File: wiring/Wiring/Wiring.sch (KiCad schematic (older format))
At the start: 9 parts, among them U1 MAIN, U2 E, U3 F, U4 G

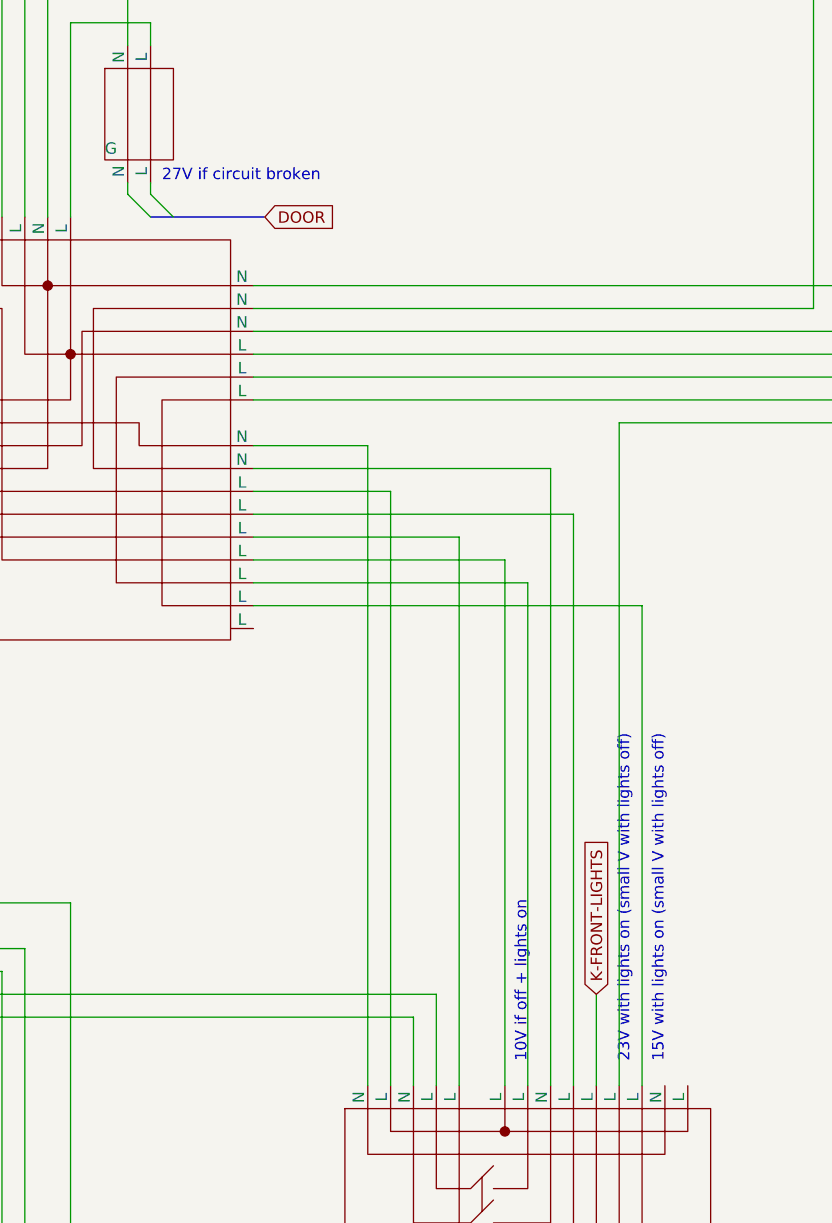
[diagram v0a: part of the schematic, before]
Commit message: Remove remarks about phantom voltage
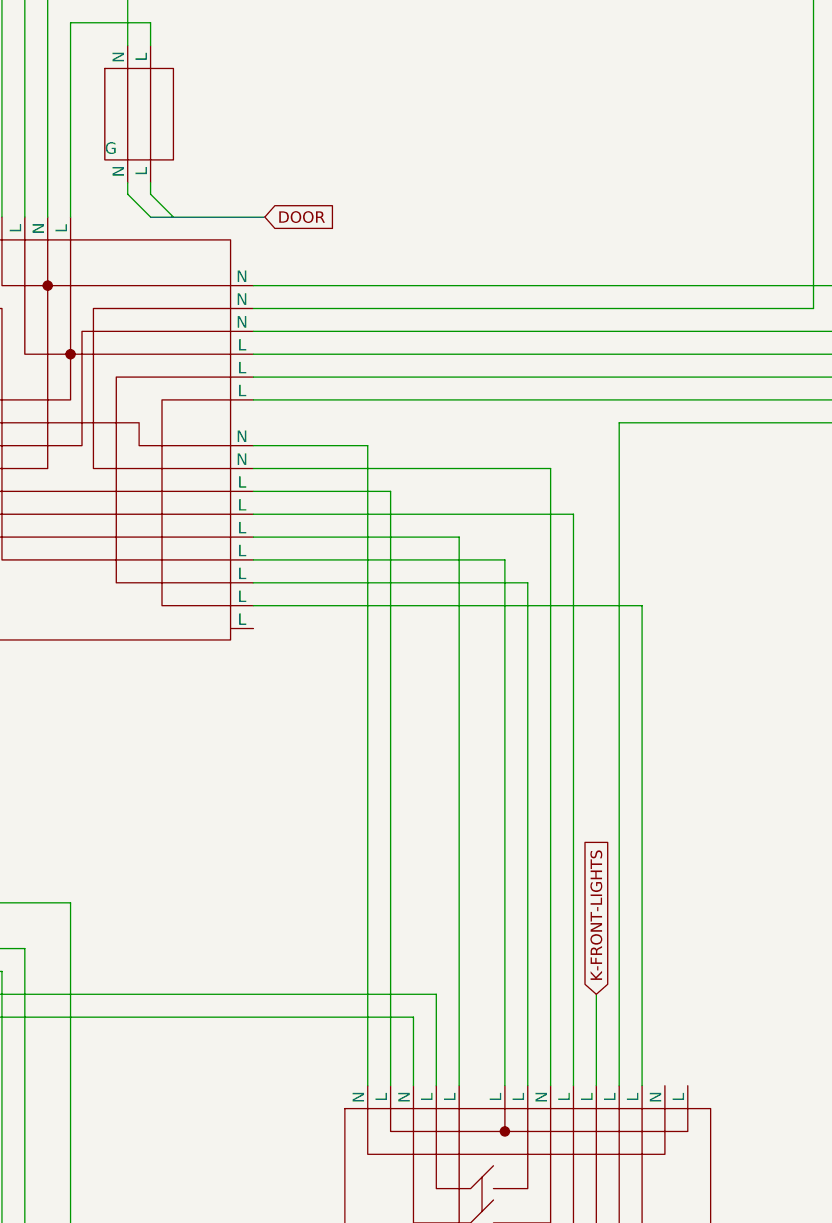
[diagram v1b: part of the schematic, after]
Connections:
- net at U3.9 (N): now also U2.17 (N)
- net at U3.~ (L): now also U2.24 (L)
- net at U2.24 (L): no longer U3.~ (L)
- net at U1.~ (N): now also U?.16 (N)
- net at U?.16 (N): no longer U1.~ (N)
- net at U?.~ (N): now also U?.12 (L)
- new net: U2.14 (L), U?.12 (L)
- new net: U?.10 (N), U?.8 (N) (x2)
- new net: U?.12 (L), U?.9 (L) (x2)
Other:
- note removed: "10V if off + lights on"
- note removed: "15V with lights on (small V with lights off)"
- note removed: "23V with lights on (small V with lights off)"
- note removed: "27V if circuit broken"
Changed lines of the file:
@@
 Text GLabel 13000 8000 1    50   Input ~ 0
 K-FRONT-LIGHTS
-Text Notes 12700 8300 1    50   ~ 0
-10V if off + lights on
-Text Notes 13150 8300 1    50   ~ 0
-23V with lights on (small V with lights off)
 Wire Wire Line
 	10300 8100 12200 8100
@@
 Wire Wire Line
 	12400 6000 12400 8400
-Text Notes 11100 4450 0    50   ~ 0
-27V if circuit broken
 Wire Notes Line
 	15600 6750 16100 6750
@@
 	-1   0    0    1
 $EndComp
-Text Notes 13300 8300 1    50   ~ 0
-15V with lights on (small V with lights off)
 Wire Wire Line
 	14450 5400 14450 2150

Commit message: Connect L, U, V
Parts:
- added U?: L, symbol Wiring:L
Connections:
- net at U3.9 (N): now also U?.12 (N)
- net at U3.~ (L): now also U?.10 (N)
- net at U2.24 (L): no longer U3.~ (L)
- net at U1.~ (N): now also U?.16 (N)
- net at U?.16 (N): no longer U1.~ (N)
- net at U?.~ (N): now also U?.12 (L)
- new net: U2.24 (L), U3.~ (L)
- new net: U2.14 (L), U?.12 (L)
- new net: U?.10 (N), U?.8 (N) (x2)
- new net: U?.12 (L), U?.9 (L) (x2)
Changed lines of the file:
@@
 Wire Wire Line
 	14550 2950 15800 2950
+$Comp
+L Wiring:L U?
+U 1 1 5EE0BFE0
+P 15250 6250
+F 0 "U?" H 15100 6400 50  0001 C CNN
+F 1 "L" H 15250 6523 50  0000 C CNN
+F 2 "" H 14550 6100 50  0001 C CNN
+F 3 "" H 14550 6100 50  0001 C CNN
+	1    15250 6250
+	1    0    0    -1
+$EndComp
+Wire Wire Line
+	13400 8400 13400 6300
+Wire Wire Line
+	13400 6300 14950 6300
+Wire Wire Line
+	13300 6200 14950 6200
+Wire Wire Line
+	13300 6200 13300 8400
+Wire Wire Line
+	15550 6200 15650 6200
+Wire Wire Line
+	15550 6300 15750 6300
+Wire Wire Line
+	15750 6300 15750 6200
+Entry Wire Line
+	15650 6200 15750 6100
+Entry Wire Line
+	15750 6200 15850 6100
 Wire Bus Line
 	10850 1850 11400 1850
@@
 Wire Bus Line
 	11050 4600 11550 4600
+Wire Bus Line
+	15750 6100 15950 6100
+Text GLabel 15950 6100 2    50   Input ~ 0
+LASER-LAB
 $EndSCHEMATC

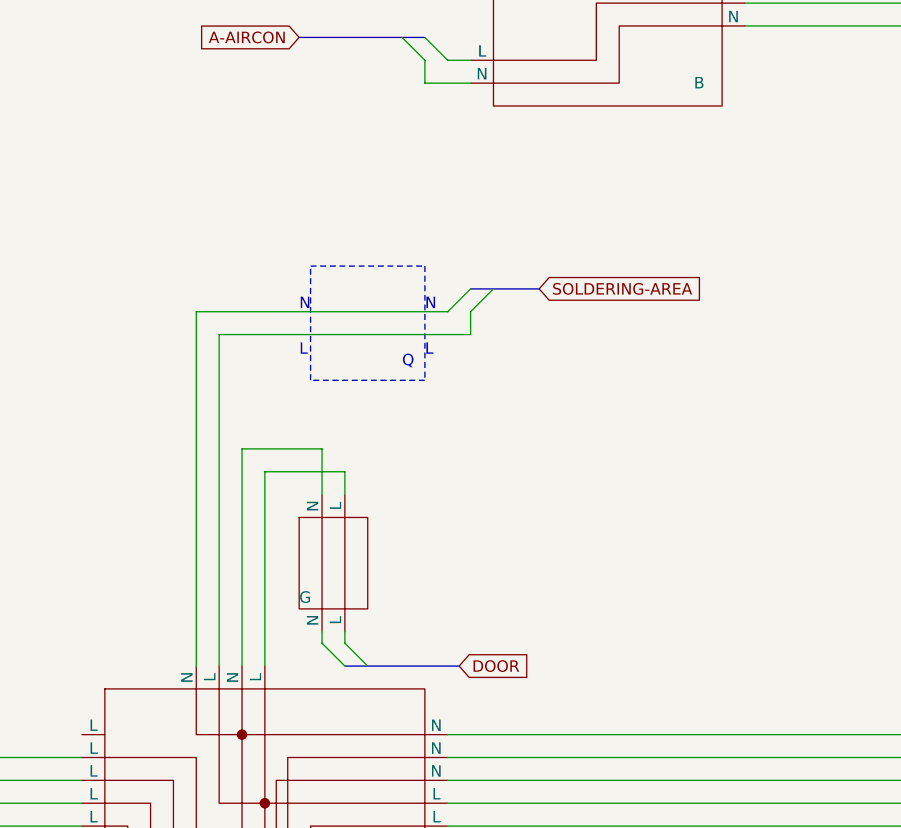
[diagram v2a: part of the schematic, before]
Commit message: Add symbol for Q
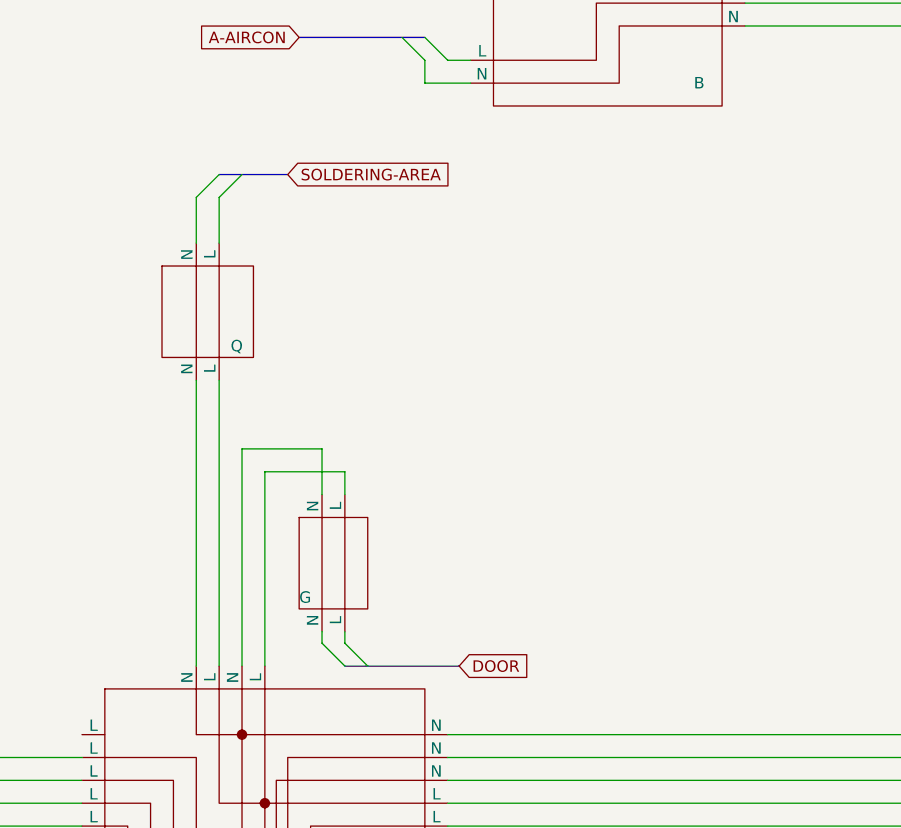
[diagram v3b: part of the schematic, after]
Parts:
- added U?: Q, symbol Wiring:Q
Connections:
- net at U3.~ (L): now also U?.10 (N); no longer U2.24 (L)
- net at U?.10 (N): no longer U3.~ (L)
- net at U2.~ (N): now also U?.12 (N)
- net at U1.~ (N): now also U?.16 (N)
- net at U?.16 (N): no longer U1.~ (N)
- net at U?.~ (N): now also U?.12 (L)
- new net: U2.24 (L), U3.~ (L)
- new net: U2.14 (L), U?.12 (L)
- new net: U2.~ (N), U?.10 (N)
- new net: U?.10 (N), U?.8 (N) (x2)
- new net: U?.12 (L), U?.9 (L) (x2)
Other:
- note removed: "Q"
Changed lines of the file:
@@
 Wire Wire Line
 	10700 7600 10700 11450
-Wire Notes Line
-	10900 2850 11400 2850
-Wire Notes Line
-	11400 2850 11400 3350
-Wire Notes Line
-	11400 3350 10900 3350
-Wire Notes Line
-	10900 3350 10900 2850
-Wire Wire Line
-	10500 4600 10500 3150
-Wire Wire Line
-	10400 4600 10400 3050
-Wire Wire Line
-	10400 3050 11500 3050
-Wire Wire Line
-	11600 3150 11600 3050
-Wire Wire Line
-	10500 3150 11600 3150
-Entry Wire Line
-	11500 3050 11600 2950
-Entry Wire Line
-	11600 3050 11700 2950
-Text GLabel 11900 2950 2    50   Input ~ 0
+Wire Wire Line
+	10500 4600 10500 3350
+Wire Wire Line
+	10400 4600 10400 3350
+Entry Wire Line
+	10400 2550 10500 2450
+Entry Wire Line
+	10500 2550 10600 2450
+Text GLabel 10800 2450 2    50   Input ~ 0
 SOLDERING-AREA
-Text Notes 11300 3300 0    50   ~ 0
-Q
-Text Notes 11400 3250 0    50   ~ 0
-L
-Text Notes 11400 3050 0    50   ~ 0
-N
-Text Notes 10850 3050 0    50   ~ 0
-N
-Text Notes 10850 3250 0    50   ~ 0
-L
 Wire Wire Line
 	11500 6100 12600 6100
@@
 Entry Wire Line
 	15750 6200 15850 6100
-Wire Bus Line
-	10850 1850 11400 1850
-Wire Bus Line
-	11600 2950 11900 2950
-Wire Bus Line
-	18000 7250 18350 7250
-Wire Bus Line
-	18000 6750 18350 6750
-Wire Bus Line
-	11900 700  12200 700
-Wire Bus Line
-	11050 4600 11550 4600
-Wire Bus Line
-	15750 6100 15950 6100
 Text GLabel 15950 6100 2    50   Input ~ 0
 LASER-LAB
+$Comp
+L Wiring:Q U?
+U 1 1 5EE2C972
+P 10450 3050
+F 0 "U?" H 10300 3200 50  0001 C CNN
+F 1 "Q" H 10550 2900 50  0000 L CNN
+F 2 "" H 9750 2900 50  0001 C CNN
+F 3 "" H 9750 2900 50  0001 C CNN
+	1    10450 3050
+	1    0    0    -1
+$EndComp
+Wire Wire Line
+	10500 2750 10500 2550
+Wire Wire Line
+	10400 2550 10400 2750
+Wire Bus Line
+	10850 1850 11400 1850
+Wire Bus Line
+	10500 2450 10800 2450
+Wire Bus Line
+	18000 7250 18350 7250
+Wire Bus Line
+	18000 6750 18350 6750
+Wire Bus Line
+	11900 700  12200 700
+Wire Bus Line
+	11050 4600 11550 4600
+Wire Bus Line
+	15750 6100 15950 6100
 $EndSCHEMATC

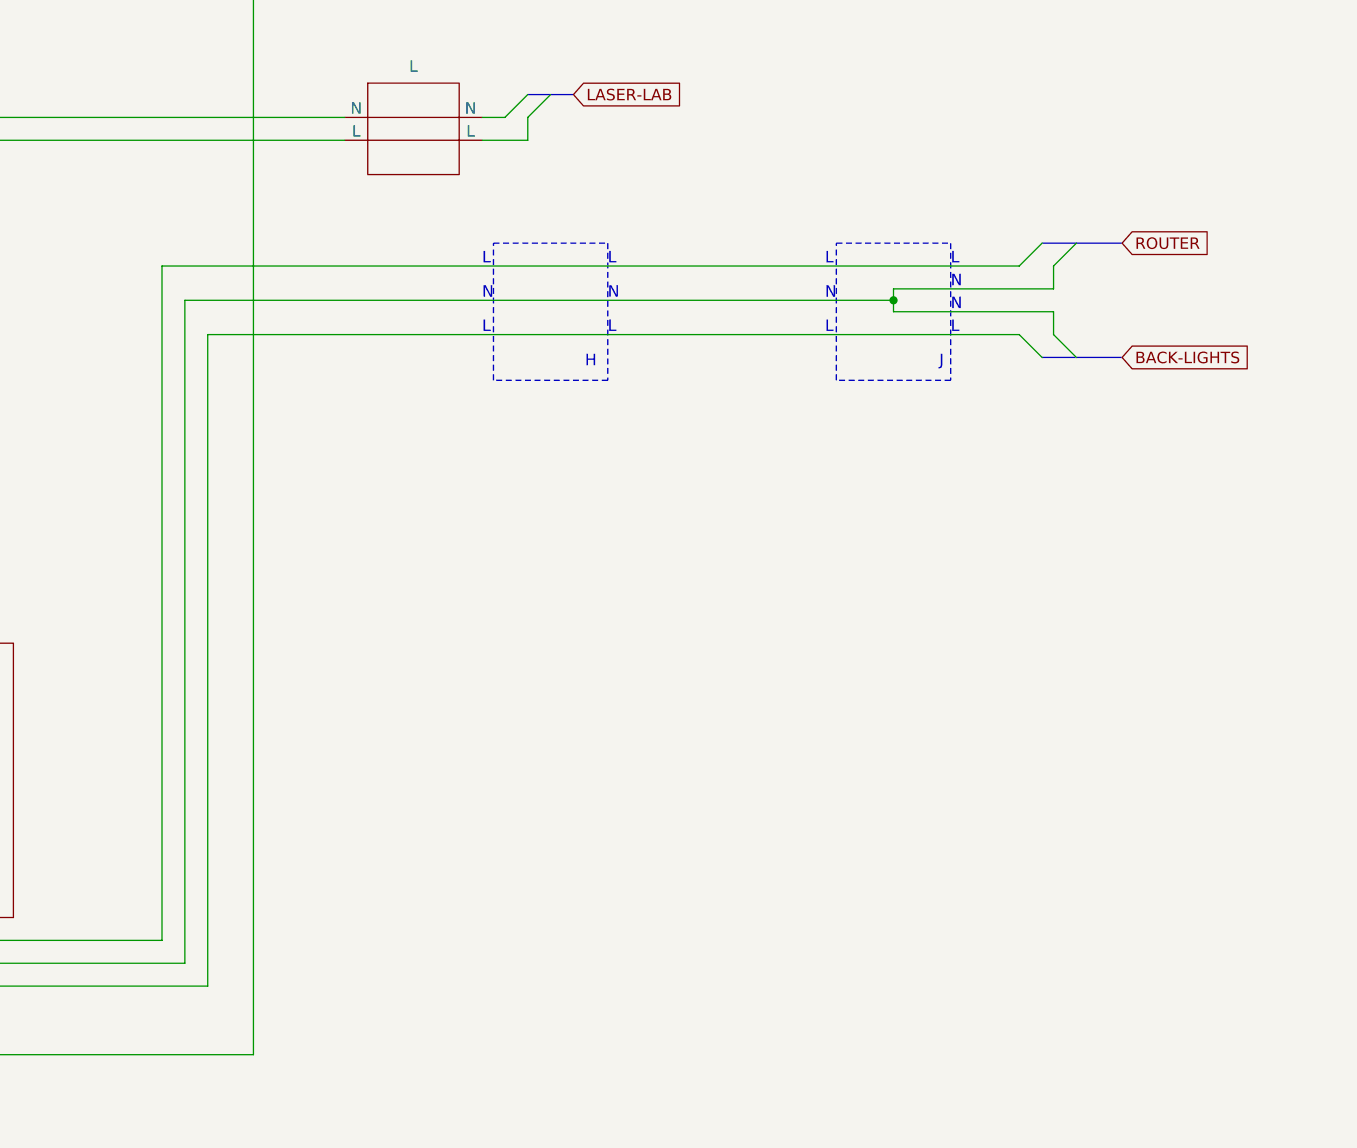
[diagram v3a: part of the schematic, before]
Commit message: Add symbol for J
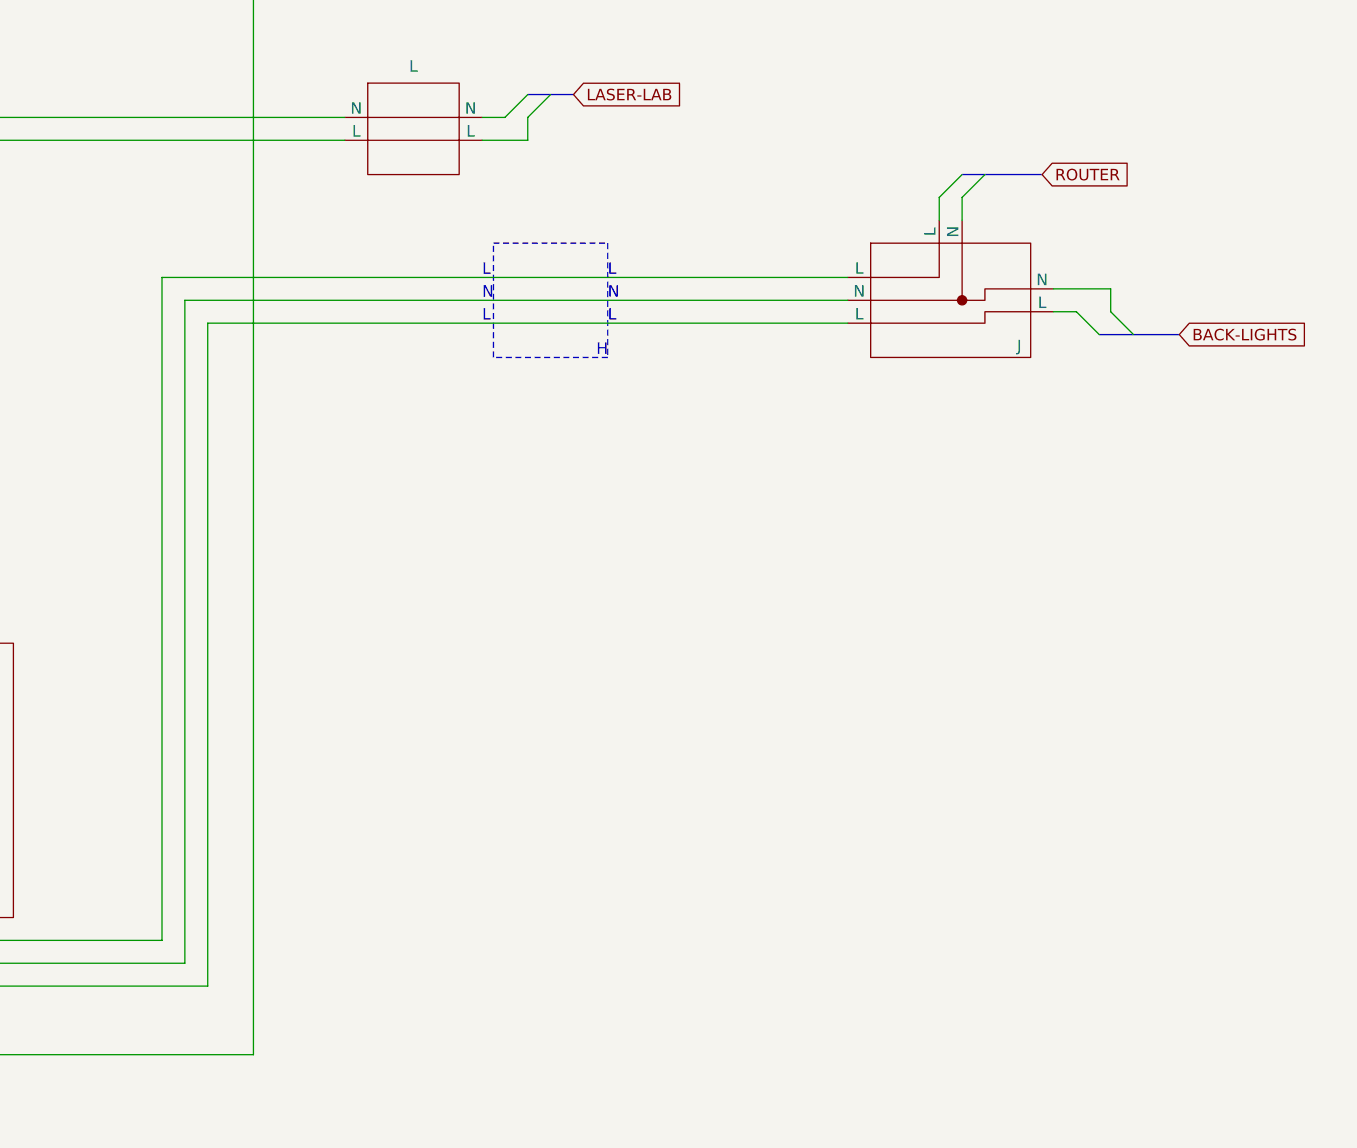
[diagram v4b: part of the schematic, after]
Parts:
- added U?: J, symbol Wiring:J
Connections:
- net at U3.~ (L): now also U?.10 (N); no longer U2.24 (L)
- net at U?.10 (N): no longer U3.~ (L)
- net at U2.6 (L): now also U?.10 (N)
- net at U2.8 (L): now also U?.10 (N)
- net at U2.~ (N): now also U?.12 (N); no longer U?.10 (N)
- net at U?.12 (N): no longer U2.~ (N)
- net at U1.~ (N): now also U?.16 (N)
- net at U?.16 (N): no longer U1.~ (N)
- net at U?.~ (N): now also U?.12 (L)
- new net: U2.24 (L), U3.~ (L)
- new net: U2.14 (L), U?.12 (L)
- new net: U2.~ (N), U?.10 (N)
- new net: U1.~ (N), U?.12 (N)
- new net: U?.10 (N), U?.8 (N) (x2)
- new net: U?.12 (L), U?.9 (L) (x2)
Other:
- note removed: "J"
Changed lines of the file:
@@
 	15600 6750 16100 6750
 Wire Notes Line
-	16100 6750 16100 7350
-Wire Notes Line
-	15600 7350 15600 6750
-Text Notes 16000 7300 0    50   ~ 0
-H
-Wire Notes Line
-	17100 6750 17600 6750
-Wire Notes Line
-	17600 6750 17600 7350
-Wire Notes Line
-	17600 7350 17100 7350
-Wire Notes Line
-	17100 7350 17100 6750
-Text Notes 17550 7300 0    50   ~ 0
-J
-Text GLabel 18350 6750 2    50   Input ~ 0
+	16100 6750 16100 7250
+Wire Notes Line
+	15600 7250 15600 6750
+Text GLabel 18000 6450 2    50   Input ~ 0
 ROUTER
 Entry Wire Line
-	17900 6850 18000 6750
-Entry Wire Line
-	18150 6750 18050 6850
-Wire Wire Line
-	18050 6950 18050 6850
+	17550 6550 17650 6450
+Entry Wire Line
+	17750 6450 17650 6550
 Wire Notes Line
 	11250 9750 11750 9750
@@
 Wire Wire Line
 	12900 5900 12900 8400
-Wire Notes Line
-	16100 7350 15600 7350
-Wire Wire Line
-	17350 6950 18050 6950
-Wire Wire Line
-	17350 7000 17350 6950
-Wire Wire Line
-	17350 7000 17350 7050
-Wire Wire Line
-	17350 7050 18050 7050
-Connection ~ 17350 7000
-Text Notes 17600 6850 0    50   ~ 0
+Text Notes 16100 6900 0    50   ~ 0
 L
-Text Notes 17600 6950 0    50   ~ 0
-N
-Text Notes 17600 7050 0    50   ~ 0
-N
-Text Notes 17600 7150 0    50   ~ 0
-L
-Text Notes 17050 6850 0    50   ~ 0
-L
-Text Notes 17050 7000 0    50   ~ 0
-N
-Text Notes 17050 7150 0    50   ~ 0
-L
-Text Notes 16100 6850 0    50   ~ 0
-L
-Text Notes 16100 7150 0    50   ~ 0
+Text Notes 16100 7100 0    50   ~ 0
 L
 Text Notes 16100 7000 0    50   ~ 0
@@
 Text Notes 15550 7000 0    50   ~ 0
 N
-Text Notes 15550 6850 0    50   ~ 0
+Text Notes 15550 6900 0    50   ~ 0
 L
-Text Notes 15550 7150 0    50   ~ 0
+Text Notes 15550 7100 0    50   ~ 0
 L
-Text GLabel 18350 7250 2    50   Input ~ 0
+Text GLabel 18600 7150 2    50   Input ~ 0
 BACK-LIGHTS
 Entry Wire Line
-	17900 7150 18000 7250
-Entry Wire Line
-	18050 7150 18150 7250
-Wire Wire Line
-	18050 7050 18050 7150
+	18150 7050 18250 7150
+Entry Wire Line
+	18300 7050 18400 7150
 Wire Wire Line
 	12300 8400 12300 8000
@@
 Wire Wire Line
 	10600 9900 14250 9900
-Wire Wire Line
-	14350 7150 14350 10000
-Wire Wire Line
-	14150 6850 14150 9800
 Wire Wire Line
 	9900 5200 9000 5200
@@
 	10800 10300 10800 11450
 Wire Wire Line
-	14150 6850 17900 6850
-Wire Wire Line
-	14250 7000 17350 7000
-Wire Wire Line
-	14350 7150 17900 7150
-Wire Wire Line
 	14550 2950 15800 2950
 $Comp
@@
 Wire Wire Line
 	10400 2550 10400 2750
+$Comp
+L Wiring:J U?
+U 1 1 5EE46860
+P 17600 7000
+F 0 "U?" H 17300 7200 50  0001 C CNN
+F 1 "J" H 17900 6800 50  0000 C CNN
+F 2 "" H 16800 6850 50  0001 C CNN
+F 3 "" H 16800 6850 50  0001 C CNN
+	1    17600 7000
+	1    0    0    -1
+$EndComp
+Wire Wire Line
+	18300 7050 18300 6950
+Wire Wire Line
+	18300 6950 18050 6950
+Wire Wire Line
+	18050 7050 18150 7050
+Wire Wire Line
+	17650 6650 17650 6550
+Wire Wire Line
+	17550 6550 17550 6650
+Wire Wire Line
+	14150 6900 14150 9800
+Wire Wire Line
+	14250 7000 17150 7000
+Wire Wire Line
+	14350 7100 14350 10000
+Text Notes 16050 7250 0    50   ~ 0
+H
+Wire Notes Line
+	16100 7250 15600 7250
+Wire Wire Line
+	17150 6900 14150 6900
+Wire Wire Line
+	17150 7100 14350 7100
+Wire Bus Line
+	15750 6100 15950 6100
 Wire Bus Line
 	10850 1850 11400 1850
@@
 	10500 2450 10800 2450
 Wire Bus Line
-	18000 7250 18350 7250
-Wire Bus Line
-	18000 6750 18350 6750
+	18250 7150 18600 7150
+Wire Bus Line
+	17650 6450 18000 6450
 Wire Bus Line
 	11900 700  12200 700
 Wire Bus Line
 	11050 4600 11550 4600
-Wire Bus Line
-	15750 6100 15950 6100
 $EndSCHEMATC
